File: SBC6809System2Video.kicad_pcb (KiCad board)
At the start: 4 copper layers, 135.4 x 101.9 mm, 70 parts, among them J1 DIN-9, J10 Conn_01x04, J11 Audio, J12 Conn_01x08, J13 Conn_01x08, J14 Conn_01x08, J15 Conn_01x08, J16 Conn_01x16, J17 Conn_01x08, J18 Conn_01x06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

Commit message: redesign
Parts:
- removed U3: 74LVC1G10, PCM_Package_TO_SOT_SMD_AKL:SOT-23-6_Handsoldering
- added C21: 100nF, PCM_Capacitor_SMD_AKL:C_0805_2012Metric_Pad1.15x1.40mm, F.Cu at (87.1, 47.8)
- added C22: 100nF, PCM_Capacitor_SMD_AKL:C_0805_2012Metric_Pad1.15x1.40mm, F.Cu at (100.6, 46.7)
- added C23: 100nF, PCM_Capacitor_SMD_AKL:C_0805_2012Metric_Pad1.15x1.40mm, F.Cu at (116.1, 47.1)
- added C24: 100nF, PCM_Capacitor_SMD_AKL:C_0805_2012Metric_Pad1.15x1.40mm, F.Cu at (123.1, 110.4)
- added C25: 100nF, PCM_Capacitor_SMD_AKL:C_0805_2012Metric_Pad1.15x1.40mm, F.Cu at (122.7, 115.4)
- added C26: 100nF, PCM_Capacitor_SMD_AKL:C_0805_2012Metric_Pad1.15x1.40mm, F.Cu at (112.4, 115.4)
- added U10: 74LS157, Package_SO:SOIC-16_3.9x9.9mm_P1.27mm, F.Cu at (108.1, 51.1)
- added U11: 74LS157, Package_SO:SOIC-16_3.9x9.9mm_P1.27mm, F.Cu at (93.9, 51.1)
- added U12: 74LS157, Package_SO:SOIC-16_3.9x9.9mm_P1.27mm, F.Cu at (128.8, 68.4)
- added U13: 74LS157, Package_SO:SOIC-16_3.9x9.9mm_P1.27mm, F.Cu at (128.8, 60.0)
- added U14: 74LS157, Package_SO:SOIC-16_3.9x9.9mm_P1.27mm, F.Cu at (107.3, 118.8)
- added U15: 27C64, Package_DIP:DIP-28_W15.24mm, F.Cu at (119.0, 95.2)
- added U16: 74LS157, Package_SO:SOIC-16_3.9x9.9mm_P1.27mm, F.Cu at (117.5, 118.8)
- U1: value IDT7006L -> IDT7006L35J
- U6: value AD724 -> AD725
- moved U9 61.1 mm to (77.5, 48.4)
- moved C14 39.7 mm to (100.7, 55.6), turned to 90 degrees
- moved U1 31.6 mm to (90.6, 74.0)
- moved C16 31.4 mm to (102.5, 91.4)
- moved C17 31.4 mm to (107.4, 91.4)
- moved C5 29.9 mm to (105.7, 135.3)
- moved C7 29.9 mm to (122.6, 131.3)
- moved C4 29.9 mm to (113.0, 125.5)
- moved U2 29.9 mm to (114.6, 134.7)
- moved C6 29.7 mm to (117.8, 142.6)
- moved J11 29.7 mm to (79.3, 88.5)
- moved U7 28.0 mm to (145.2, 125.5)
- moved U8 28.0 mm to (135.2, 126.1)
- moved C15 27.4 mm to (84.8, 79.1)
- moved C10 27.1 mm to (66.7, 137.6)
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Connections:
- U1 pad 1: /MA13 -> /XA13
- U1 pad 34: /PB5 -> /PA7
- U1 pad 55: /MA0 -> /XA0
- U1 pad 56: /MA1 -> /XA1
- U1 pad 57: /MA2 -> /XA2
- U1 pad 58: /MA3 -> /XA3
- U1 pad 59: /MA4 -> /XA4
- U1 pad 60: /MA5 -> /XA5
- U1 pad 61: /MA6 -> /XA6
- U1 pad 62: /MA7 -> /XA7
- U1 pad 63: /MA8 -> /XA8
- U1 pad 64: /MA9 -> /XA9
- U1 pad 65: /MA10 -> /XA10
- U1 pad 66: /MA11 -> /XA11
- U1 pad 67: /MA12 -> /XA12
- U2 pad 12: /MD7 -> /GD7
- U2 pad 13: /MD6 -> /GD6
- U2 pad 14: /MD5 -> /GD5
- U2 pad 15: /MD4 -> /GD4
- U2 pad 18: /MD3 -> /GD3
- U2 pad 20: /MD2 -> /GD2
- U2 pad 21: /MD0 -> /GD1
- U2 pad 22: /MD1 -> /GD0
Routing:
- net /PB1: track 0.00 -> 198.6 mm, vias 0 -> 7
- net R/~{W}: track 220.9 -> 349.7 mm, vias 3 -> 4
- net D0: track 189.8 -> 318.3 mm, vias 2 -> 5
- net A1: track 143.5 -> 258.8 mm
- net /RA0: track 0.00 -> 110.8 mm, vias 0 -> 3
- net /RA1: track 0.00 -> 109.7 mm, vias 0 -> 3
- net ~{IRQ}: track 123.6 -> 232.1 mm
- net /RA2: track 0.00 -> 102.6 mm, vias 0 -> 3
- net A9: track 108.9 -> 207.6 mm, vias 3 -> 1
- net A10: track 112.4 -> 209.6 mm, vias 3 -> 1
- net A11: track 110.8 -> 207.0 mm, vias 3 -> 1
- net A8: track 112.9 -> 207.3 mm, vias 3 -> 1
- net D6: track 179.4 -> 267.4 mm, vias 2 -> 4
- net D4: track 181.5 -> 269.0 mm, vias 2 -> 4
- net D5: track 181.5 -> 268.1 mm, vias 2 -> 4
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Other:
- board size 135.4 x 101.9 mm -> 161.3 x 101.9 mm

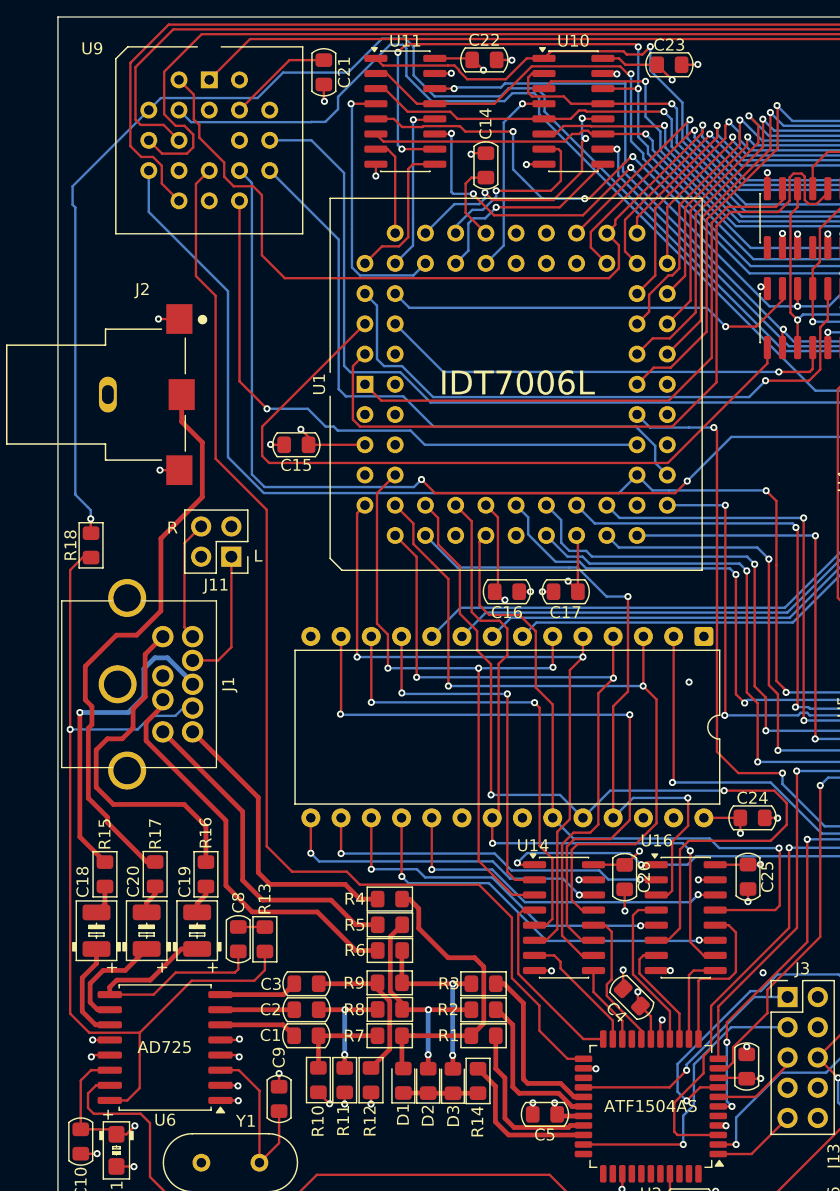
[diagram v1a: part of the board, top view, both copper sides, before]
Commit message: fix missing U3
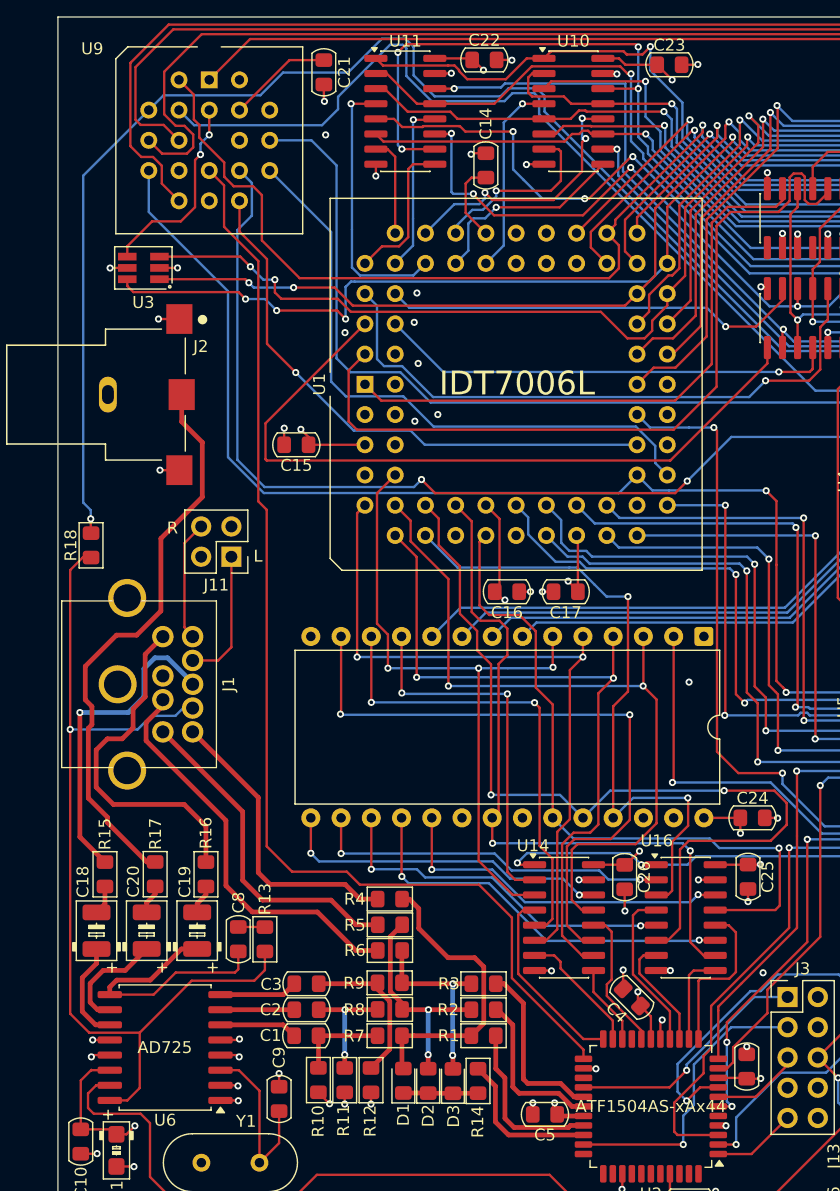
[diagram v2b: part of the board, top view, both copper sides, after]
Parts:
- added U3: 74LVC1G10, PCM_Package_TO_SOT_SMD_AKL:SOT-23-6_Handsoldering, F.Cu at (71.9, 64.2)
- U2: value ATF1504AS -> ATF1504AS-xAx44
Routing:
- net A5: track 197.1 -> 247.7 mm, vias 1 -> 4
- net A7: track 200.3 -> 249.1 mm, vias 1 -> 3
- net A6: track 203.5 -> 245.0 mm, vias 1 -> 3
- net /~{SELPH}: track 0.00 -> 16.6 mm, vias 0 -> 2
- net /MEM_CE: track 50.8 -> 47.6 mm
- net GND: track 69.6 -> 71.4 mm, vias 57 -> 65
- net /BLANK: track 97.9 -> 96.2 mm
- net +5V: track 111.2 -> 112.8 mm, vias 23 -> 24
- net /XA12: track 66.7 -> 67.7 mm
- net /PIA: track 141.1 -> 142.1 mm
- net /~{HS}: track 145.3 -> 144.5 mm
- net A2: track 251.9 -> 251.2 mm

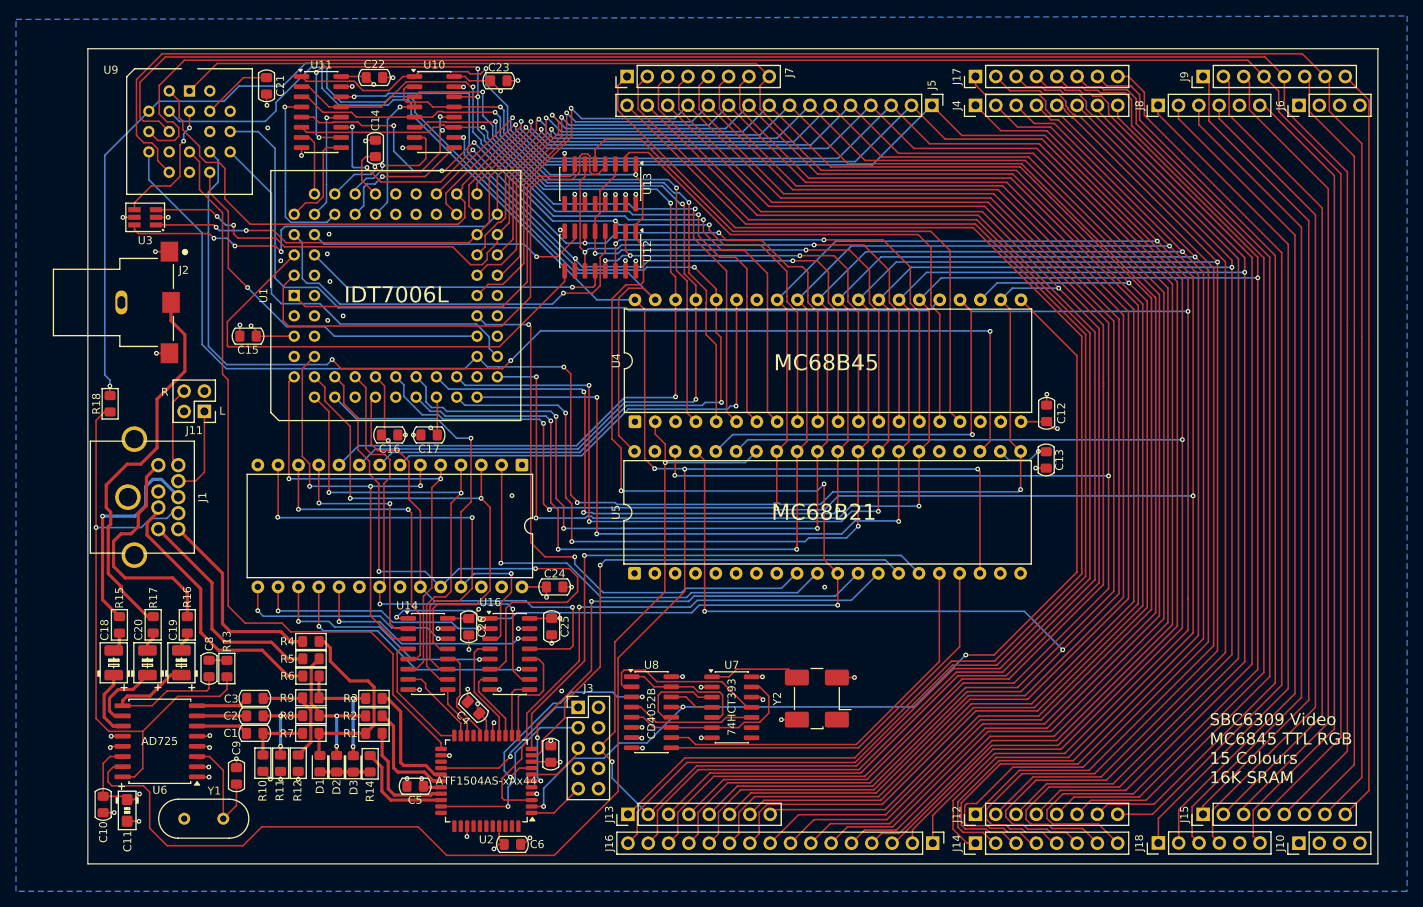
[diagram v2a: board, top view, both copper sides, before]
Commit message: update fabrication details
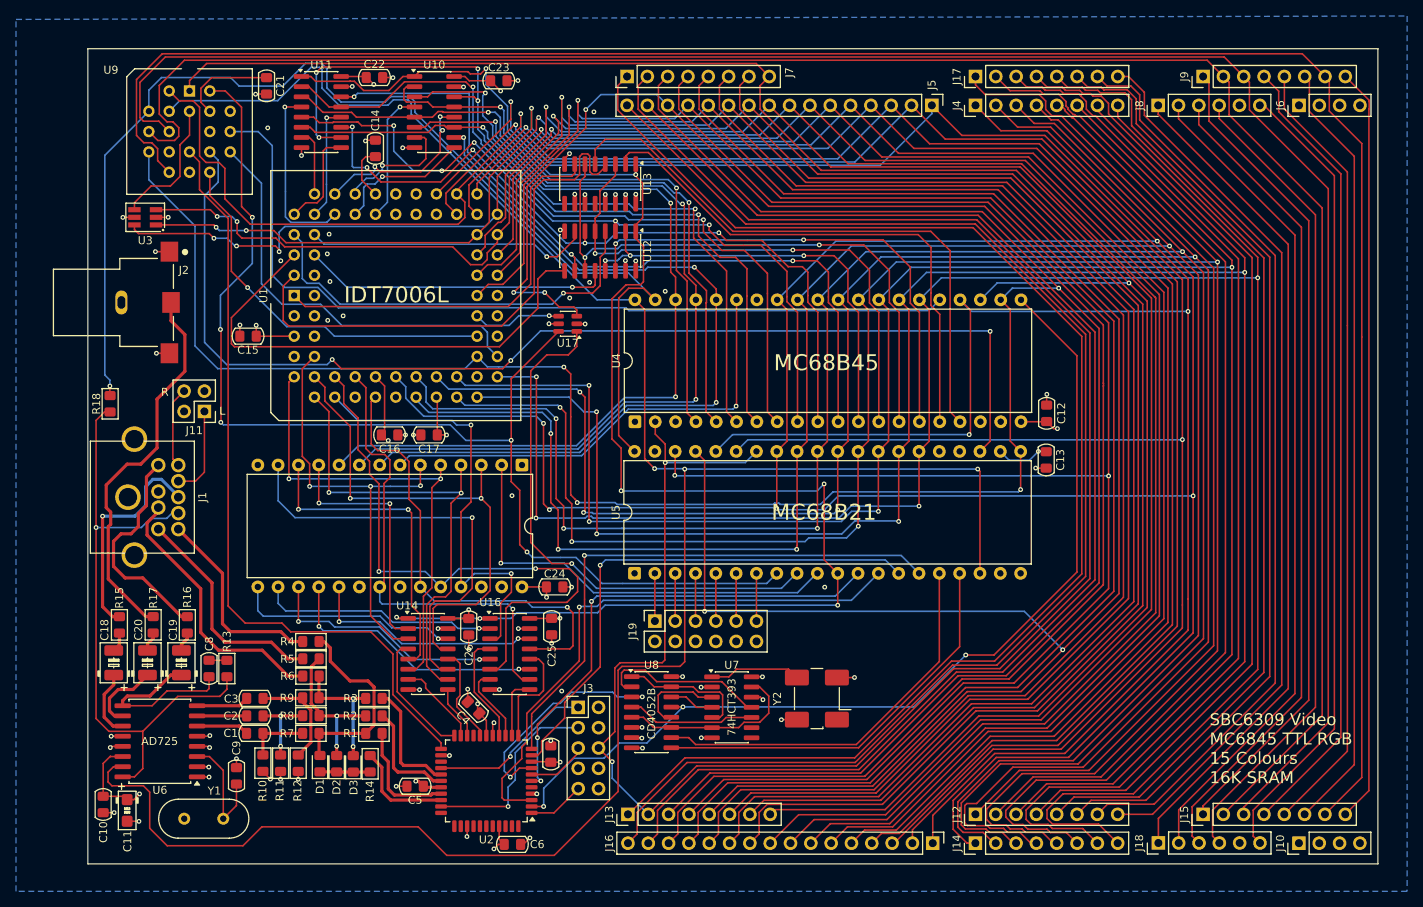
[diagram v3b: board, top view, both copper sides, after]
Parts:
- added J19: Spare, Connector_PinSocket_2.54mm:PinSocket_2x06_P2.54mm_Vertical, F.Cu at (135.6, 114.7)
- added U17: TS5A63157DBV, Package_TO_SOT_SMD:SOT-23-6, F.Cu at (124.7, 77.5)
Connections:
- U1 pad 34: /PA7 -> /EXA13
- U9 pad 19: unconnected-(U9-IO1-Pad19) -> /PA6
- U9 pad 6: DEV3 -> DEV1
- U9 pad 7: DEV4 -> DEV2
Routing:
- net DEV4: track 252.9 -> 98.8 mm
- net DEV3: track 252.6 -> 100.2 mm
- net DEV2: track 101.0 -> 250.1 mm
- net /PA6: track 0.00 -> 147.9 mm, vias 0 -> 5
- net DEV1: track 102.5 -> 249.8 mm
- net A13: track 167.6 -> 215.4 mm, vias 0 -> 3
- net /EXA13: track 0.00 -> 11.2 mm, vias 0 -> 1
- net /PA5: track 0.00 -> 6.02 mm
- net /PA3: track 0.00 -> 6.02 mm
- net /PA2: track 0.00 -> 6.02 mm
- net /PA0: track 0.00 -> 6.02 mm
- net /PA4: track 0.00 -> 6.02 mm
- net /PA1: track 0.00 -> 6.02 mm
- net A10: track 209.8 -> 214.8 mm
- net /PA7: track 71.7 -> 66.8 mm, vias 2 -> 1
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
